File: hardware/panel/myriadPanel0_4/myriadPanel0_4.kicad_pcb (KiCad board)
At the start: 2 copper layers, 81.7 x 128.9 mm, 24 parts

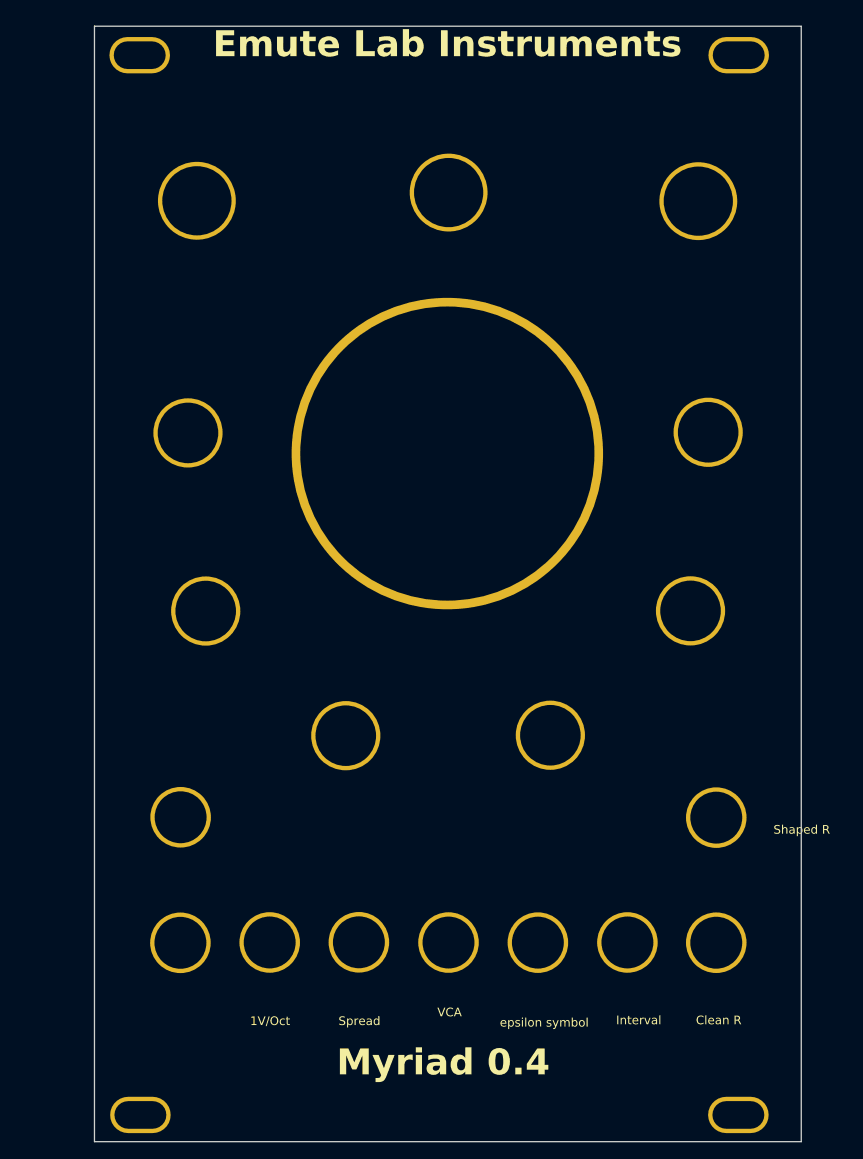
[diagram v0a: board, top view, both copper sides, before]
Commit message: adc oversampling
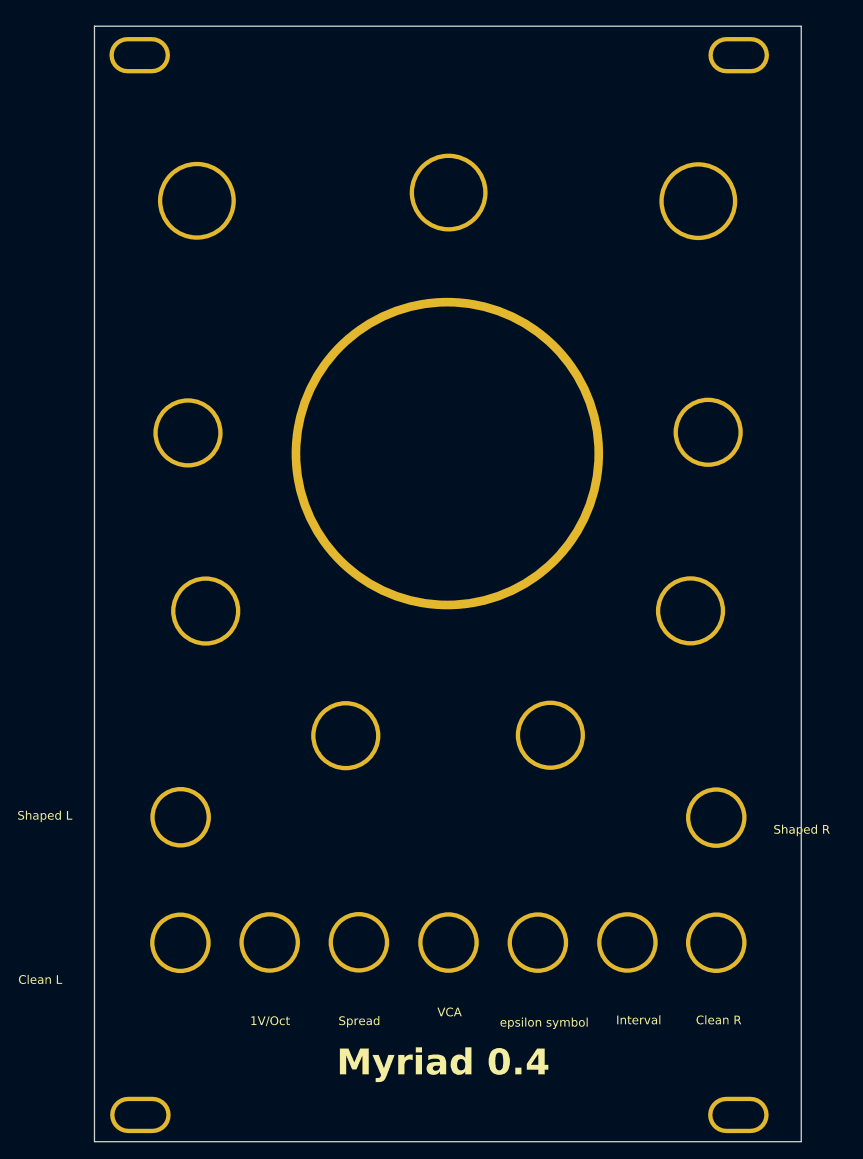
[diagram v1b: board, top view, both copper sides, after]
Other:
- board text removed: "Emute Lab Instruments"
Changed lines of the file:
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@@
+		)
+	)
+	(gr_text "Clean L\n"
+		(at 37.91 134.47 0)
+		(layer "F.SilkS")
+		(effects
+			(font
+				(size 1 1)
+				(thickness 0.15)
+			)
+			(justify left bottom)
 		)
 	)
@@
 	(gr_text "Myriad 0.4\n\n"
 		(at 74.71 150.01 0)
-		(layer "F.SilkS" knockout)
-		(effects
-			(font
-				(size 3 3)
-				(thickness 0.3)
-				(bold yes)
-			)
-			(justify left bottom)
-		)
-	)
-	(gr_text "Emute Lab Instruments"
-		(at 60.4 27.48 0)
 		(layer "F.SilkS" knockout)
 		(effects
@@
 		)
 	)
-	(gr_text "Clean R\n"
-		(at 116.24 139.14 0)
+	(gr_text "Shaped L"
+		(at 37.8 115.49 0)
 		(layer "F.SilkS")
 		(effects
@@
 		)
 	)
-	(gr_text "Clean L\n"
-		(at 37.91 134.47 0)
-		(layer "Dwgs.User")
+	(gr_text "Clean R\n"
+		(at 116.24 139.14 0)
+		(layer "F.SilkS")
 		(effects
 			(font
-				(size 1 1)
-				(thickness 0.15)
-			)
-			(justify left bottom)
-		)
-	)
-	(gr_text "Shaped L"
-		(at 37.8 115.49 0)
-		(layer "Dwgs.User")
-		(effects
-			(font
